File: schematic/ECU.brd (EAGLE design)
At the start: 24 x 72 mm, 29 parts, among them J1 Break, J2 COMM, J3 PWR, J4 DISPLAY, J5 THROTTLE, J6 LED, J7 SPEED, Q1 NMOSFETSOT23, Q5 NMOSFETSOT23, U1 Arduino Nano Every

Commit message: Invert stop pin logic according to new schematics
- Invert stop pin logic to use high-side p-mosfet switch
- Update TVS diode symbol
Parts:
- Q1, Q5: value NMOSFETSOT23 -> NMOSFET
- Q2: value (none) -> NMOSFET
- Q4: value (none) -> BSS84
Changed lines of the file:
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@@
 <attribute name="VALUE" x="-0.032" y="52.07" size="0.6096" layer="27" font="vector" ratio="20" rot="R270"/>
 </element>
-<element name="Q1" library="Transistor" library_urn="urn:adsk.eagle:library:16378713" package="SOT23" package3d_urn="urn:adsk.eagle:package:28738/2" value="NMOSFETSOT23" x="6.69" y="65.15" smashed="yes" rot="MR270">
+<element name="Q1" library="Transistor" library_urn="urn:adsk.eagle:library:16378713" package="SOT23" package3d_urn="urn:adsk.eagle:package:28738/2" value="NMOSFET" x="6.69" y="65.15" smashed="yes" rot="MR270">
 <attribute name="CATEGORY" value="Transistor" x="66.38" y="8" size="1.778" layer="28" rot="MR270" display="off"/>
 <attribute name="DESCRIPTION" value="" x="66.38" y="8" size="1.778" layer="28" rot="MR270" display="off"/>
@@
 <attribute name="THERMALLOSS" value="" x="66.38" y="8" size="1.778" layer="28" rot="MR270" display="off"/>
 <attribute name="TYPE" value="N-Channel" x="66.38" y="8" size="1.778" layer="28" rot="MR270" display="off"/>
-<attribute name="VALUE" x="9.865" y="67.055" size="1.27" layer="28" rot="MR270"/>
+<attribute name="VALUE" value="NMOSFET" x="9.865" y="67.055" size="1.27" layer="28" rot="MR270"/>
 </element>
-<element name="Q2" library="Transistor" library_urn="urn:adsk.eagle:library:16378713" package="SOT23" package3d_urn="urn:adsk.eagle:package:28738/2" value="" x="4" y="15.66" smashed="yes" rot="MR0">
+<element name="Q2" library="Transistor" library_urn="urn:adsk.eagle:library:16378713" package="SOT23" package3d_urn="urn:adsk.eagle:package:28738/2" value="NMOSFET" x="4" y="15.66" smashed="yes" rot="MR0">
 <attribute name="CATEGORY" value="Transistor" x="-21.4" y="-58" size="1.778" layer="28" rot="MR0" display="off"/>
 <attribute name="DESCRIPTION" value="" x="-21.4" y="-58" size="1.778" layer="28" rot="MR0" display="off"/>
@@
 <attribute name="THERMALLOSS" value="" x="-21.4" y="-58" size="1.778" layer="28" rot="MR0" display="off"/>
 <attribute name="TYPE" value="N-Channel" x="-21.4" y="-58" size="1.778" layer="28" rot="MR0" display="off"/>
-<attribute name="VALUE" x="5.905" y="12.485" size="1.27" layer="28" rot="MR0"/>
+<attribute name="VALUE" value="NMOSFET" x="5.905" y="12.485" size="1.27" layer="28" rot="MR0"/>
 </element>
-<element name="Q4" library="Transistor" library_urn="urn:adsk.eagle:library:16378713" package="SOT23" package3d_urn="urn:adsk.eagle:package:28738/2" value="" x="2.52" y="23.66" smashed="yes" rot="MR0">
+<element name="Q4" library="Transistor" library_urn="urn:adsk.eagle:library:16378713" package="SOT23" package3d_urn="urn:adsk.eagle:package:28738/2" value="BSS84" x="2.52" y="23.66" smashed="yes" rot="MR0">
 <attribute name="CATEGORY" value="Transistor" x="-27.96" y="-50" size="1.778" layer="28" rot="MR0" display="off"/>
 <attribute name="DESCRIPTION" value="MOSFET P-CH 50V 130MA SOT-23" x="-27.96" y="-50" size="1.778" layer="28" rot="MR0" display="off"/>
-<attribute name="DRAIN_CURRENT" value="" x="-27.96" y="-50" size="1.778" layer="28" rot="MR0" display="off"/>
+<attribute name="DRAIN_CURRENT" value="130mA" x="-27.96" y="-50" size="1.778" layer="28" rot="MR0" display="off"/>
 <attribute name="MANUFACTURER" value="ON Semiconductor" x="-27.96" y="-50" size="1.778" layer="28" rot="MR0" display="off"/>
 <attribute name="MPN" value="BSS84" x="-27.96" y="-50" size="1.778" layer="28" rot="MR0" display="off"/>
 <attribute name="NAME" x="4.425" y="25.565" size="1.27" layer="26" rot="MR0"/>
-<attribute name="OPERATING_TEMP" value="" x="-27.96" y="-50" size="1.778" layer="28" rot="MR0" display="off"/>
-<attribute name="PART_STATUS" value="" x="-27.96" y="-50" size="1.778" layer="28" rot="MR0" display="off"/>
-<attribute name="ROHS_COMPLIANT" value="" x="-27.96" y="-50" size="1.778" layer="28" rot="MR0" display="off"/>
+<attribute name="OPERATING_TEMP" value="-55°C ~ 150°C" x="-27.96" y="-50" size="1.778" layer="28" rot="MR0" display="off"/>
+<attribute name="PART_STATUS" value="Active" x="-27.96" y="-50" size="1.778" layer="28" rot="MR0" display="off"/>
+<attribute name="ROHS_COMPLIANT" value="Yes" x="-27.96" y="-50" size="1.778" layer="28" rot="MR0" display="off"/>
 <attribute name="SERIES" value="" x="-27.96" y="-50" size="1.778" layer="28" rot="MR0" display="off"/>
 <attribute name="SUB-CATEGORY" value="MOSFET" x="-27.96" y="-50" size="1.778" layer="28" rot="MR0" display="off"/>
-<attribute name="THERMALLOSS" value="" x="-27.96" y="-50" size="1.778" layer="28" rot="MR0" display="off"/>
+<attribute name="THERMALLOSS" value="360mW" x="-27.96" y="-50" size="1.778" layer="28" rot="MR0" display="off"/>
 <attribute name="TYPE" value="P-Channel" x="-27.96" y="-50" size="1.778" layer="28" rot="MR0" display="off"/>
-<attribute name="VALUE" x="4.425" y="20.485" size="1.27" layer="28" rot="MR0"/>
+<attribute name="VALUE" value="BSS84" x="4.425" y="20.485" size="1.27" layer="28" rot="MR0"/>
 </element>
-<element name="Q5" library="Transistor" library_urn="urn:adsk.eagle:library:16378713" package="SOT23" package3d_urn="urn:adsk.eagle:package:28738/2" value="NMOSFETSOT23" x="18.31" y="40.67" smashed="yes" rot="MR90">
+<element name="Q5" library="Transistor" library_urn="urn:adsk.eagle:library:16378713" package="SOT23" package3d_urn="urn:adsk.eagle:package:28738/2" value="NMOSFET" x="18.31" y="40.67" smashed="yes" rot="MR90">
 <attribute name="CATEGORY" value="Transistor" x="-49" y="67.34" size="1.778" layer="28" rot="MR90" display="off"/>
 <attribute name="DESCRIPTION" value="" x="-49" y="67.34" size="1.778" layer="28" rot="MR90" display="off"/>
@@
 <attribute name="THERMALLOSS" value="" x="-49" y="67.34" size="1.778" layer="28" rot="MR90" display="off"/>
 <attribute name="TYPE" value="N-Channel" x="-49" y="67.34" size="1.778" layer="28" rot="MR90" display="off"/>
-<attribute name="VALUE" x="15.135" y="38.765" size="1.27" layer="28" rot="MR90"/>
+<attribute name="VALUE" value="NMOSFET" x="15.135" y="38.765" size="1.27" layer="28" rot="MR90"/>
 </element>
 <element name="R1" library="eagle-ltspice" library_urn="urn:adsk.eagle:library:217" package="R1206" package3d_urn="urn:adsk.eagle:package:13301/1" value="10K" x="19.5" y="51.07" smashed="yes" rot="MR90">

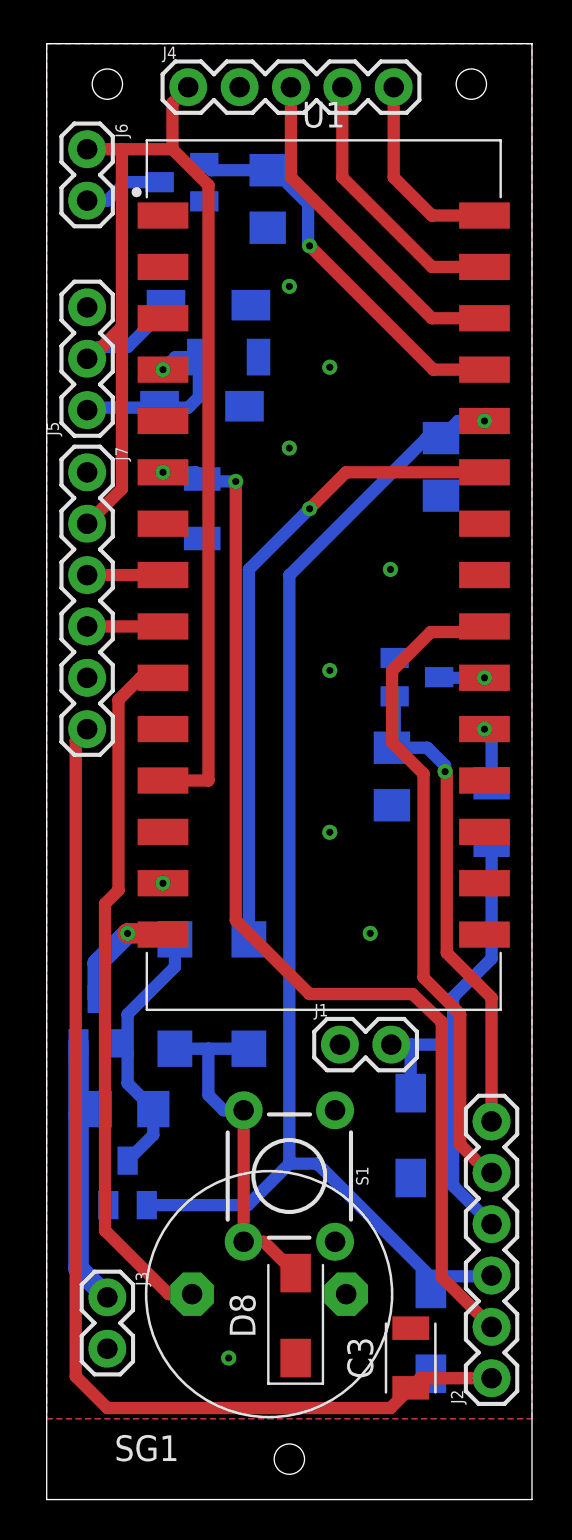
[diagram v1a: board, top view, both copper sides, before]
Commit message: Prettify ECU schematic according to #1
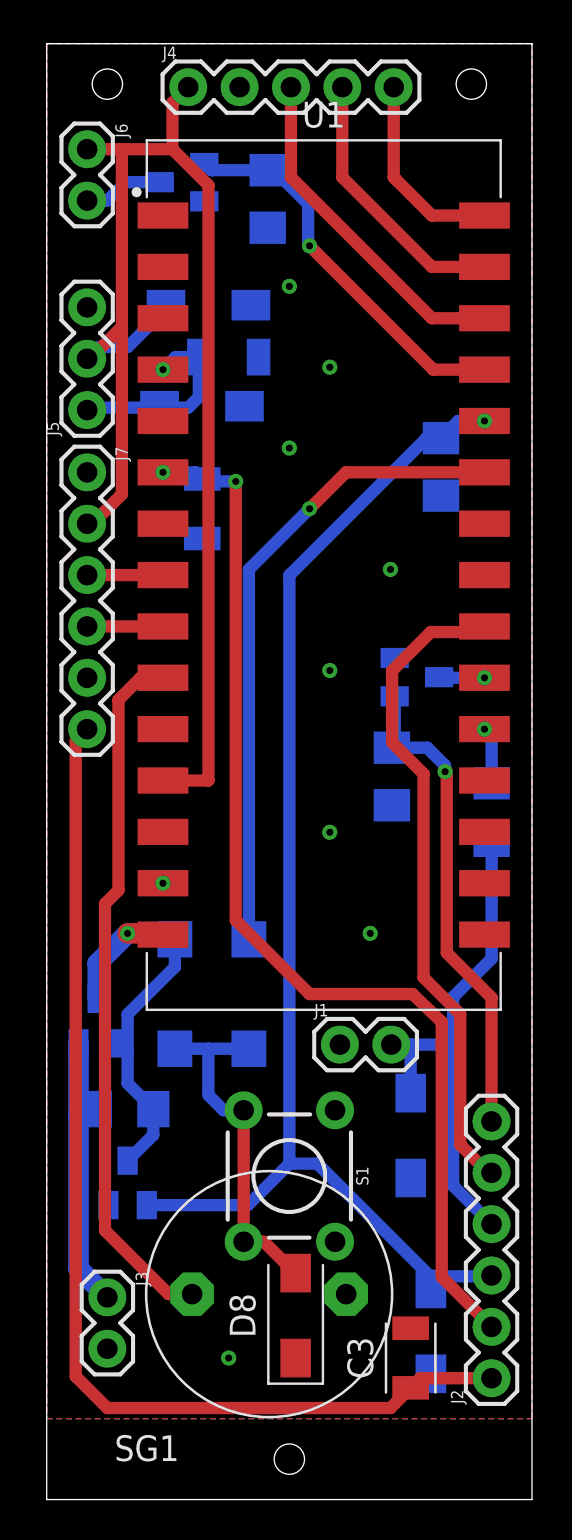
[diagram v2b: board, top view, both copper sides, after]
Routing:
- net N$2: track 13.7 -> 14.6 mm
- net SP: track 2.25 -> 2.81 mm
